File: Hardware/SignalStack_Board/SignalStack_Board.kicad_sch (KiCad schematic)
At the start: 64 parts, among them J1 Molex_uF_SV_06, J2 RJ45_LED_Shielded, J3 Molex_uF_SV_06, Q1 SI4156DY, Q2 SI4156DY, Q3 SI4156DY, Q4 SI4156DY, Q5 SI4156DY, Q6 SI4156DY, Q7 SI4156DY, Q8 SI4156DY, U1 OKI, U2 SMAJ12CA, U3 Teensy4.1_DEV-16771, U4 TSR_1-2450, U5 IRS2005S, U6 IRS2005S, U8 IRS2005S, U9 IRS2005S

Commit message: Worked on layout
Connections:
- net IMU Data is gone; now on net I2C SDA: U3.18 (A4)
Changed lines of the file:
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@@
     )
   )
-  (global_label "IMU Data" (shape input) (at 31.75 166.37 180) (fields_autoplaced)
+  (global_label "I2C SDA" (shape input) (at 31.75 166.37 180) (fields_autoplaced)
     (effects (font (size 1.27 1.27)) (justify right))
-    (property "Intersheet References" "${INTERSHEET_REFS}" (id 0) (at 20.6888 166.2906 0)
+    (property "Intersheet References" "${INTERSHEET_REFS}" (id 0) (at 21.7169 166.2906 0)
       (effects (font (size 1.27 1.27)) (justify right) hide)
     )

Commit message: Started BOM
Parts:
- Conn1, Conn2, Conn3: footprint MRDT_Connectors:Anderson_2_Horizontal_Side_by_Side -> MRDT_Connectors:Square_Anderson_2_H_Side_By_Side
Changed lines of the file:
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@@
       (effects (font (size 1.524 1.524)))
     )
-    (property "Footprint" "MRDT_Connectors:Anderson_2_Horizontal_Side_by_Side" (id 2) (at 15.24 39.37 0)
+    (property "Footprint" "MRDT_Connectors:Square_Anderson_2_H_Side_By_Side" (id 2) (at 15.24 39.37 0)
       (effects (font (size 1.524 1.524)) hide)
     )
@@
       (effects (font (size 1.524 1.524)))
     )
-    (property "Footprint" "MRDT_Connectors:Anderson_2_Horizontal_Side_by_Side" (id 2) (at 209.55 52.07 0)
+    (property "Footprint" "MRDT_Connectors:Square_Anderson_2_H_Side_By_Side" (id 2) (at 209.55 52.07 0)
       (effects (font (size 1.524 1.524)) hide)
     )
@@
       (effects (font (size 1.524 1.524)))
     )
-    (property "Footprint" "MRDT_Connectors:Anderson_2_Horizontal_Side_by_Side" (id 2) (at 209.55 102.87 0)
+    (property "Footprint" "MRDT_Connectors:Square_Anderson_2_H_Side_By_Side" (id 2) (at 209.55 102.87 0)
       (effects (font (size 1.524 1.524)) hide)
     )
@@
       (effects (font (size 1.524 1.524)))
     )
-    (property "Footprint" "MRDT_Connectors:Anderson_2_Horizontal_Side_by_Side" (id 2) (at 15.24 52.07 0)
+    (property "Footprint" "MRDT_Connectors:Square_Anderson_2_H_Side_By_Side" (id 2) (at 15.24 52.07 0)
       (effects (font (size 1.524 1.524)) hide)
     )
@@
       (effects (font (size 1.524 1.524)) (justify right))
     )
-    (property "Footprint" "MRDT_Connectors:Anderson_2_Horizontal_Side_by_Side" (id 2) (at 207.01 19.05 0)
+    (property "Footprint" "MRDT_Connectors:Square_Anderson_2_H_Side_By_Side" (id 2) (at 207.01 19.05 0)
       (effects (font (size 1.524 1.524)) hide)
     )
@@
       (effects (font (size 1.524 1.524)) (justify right))
     )
-    (property "Footprint" "MRDT_Connectors:Anderson_2_Horizontal_Side_by_Side" (id 2) (at 207.01 69.85 0)
+    (property "Footprint" "MRDT_Connectors:Square_Anderson_2_H_Side_By_Side" (id 2) (at 207.01 69.85 0)
       (effects (font (size 1.524 1.524)) hide)
     )
@@
     )
     (path "/c059550b-e967-4b7c-8d54-2cc4b7e0eff1"
-      (reference "Conn1") (unit 1) (value "AndersonPP") (footprint "MRDT_Connectors:Anderson_2_Horizontal_Side_by_Side")
+      (reference "Conn1") (unit 1) (value "AndersonPP") (footprint "MRDT_Connectors:Square_Anderson_2_H_Side_By_Side")
     )
     (path "/4470fd7a-32a9-4a7f-937a-98c8610c7077"
-      (reference "Conn1") (unit 2) (value "AndersonPP") (footprint "MRDT_Connectors:Anderson_2_Horizontal_Side_by_Side")
+      (reference "Conn1") (unit 2) (value "AndersonPP") (footprint "MRDT_Connectors:Square_Anderson_2_H_Side_By_Side")
     )
     (path "/f402e432-547b-44fa-9c6b-b785a1b7d57e"
-      (reference "Conn2") (unit 1) (value "AndersonPP") (footprint "MRDT_Connectors:Anderson_2_Horizontal_Side_by_Side")
+      (reference "Conn2") (unit 1) (value "AndersonPP") (footprint "MRDT_Connectors:Square_Anderson_2_H_Side_By_Side")
     )
     (path "/7f2e505c-6f2f-471a-8048-b70c1151c3de"
-      (reference "Conn2") (unit 2) (value "AndersonPP") (footprint "MRDT_Connectors:Anderson_2_Horizontal_Side_by_Side")
+      (reference "Conn2") (unit 2) (value "AndersonPP") (footprint "MRDT_Connectors:Square_Anderson_2_H_Side_By_Side")
     )
     (path "/f66c17f9-1ad2-418f-8418-6459a4b4a42b"
-      (reference "Conn3") (unit 1) (value "AndersonPP") (footprint "MRDT_Connectors:Anderson_2_Horizontal_Side_by_Side")
+      (reference "Conn3") (unit 1) (value "AndersonPP") (footprint "MRDT_Connectors:Square_Anderson_2_H_Side_By_Side")
     )
     (path "/b6d93951-9299-41a0-8a04-6f5e517005d6"
-      (reference "Conn3") (unit 2) (value "AndersonPP") (footprint "MRDT_Connectors:Anderson_2_Horizontal_Side_by_Side")
+      (reference "Conn3") (unit 2) (value "AndersonPP") (footprint "MRDT_Connectors:Square_Anderson_2_H_Side_By_Side")
     )
     (path "/49a02109-597c-409b-9a51-a35132935b24"

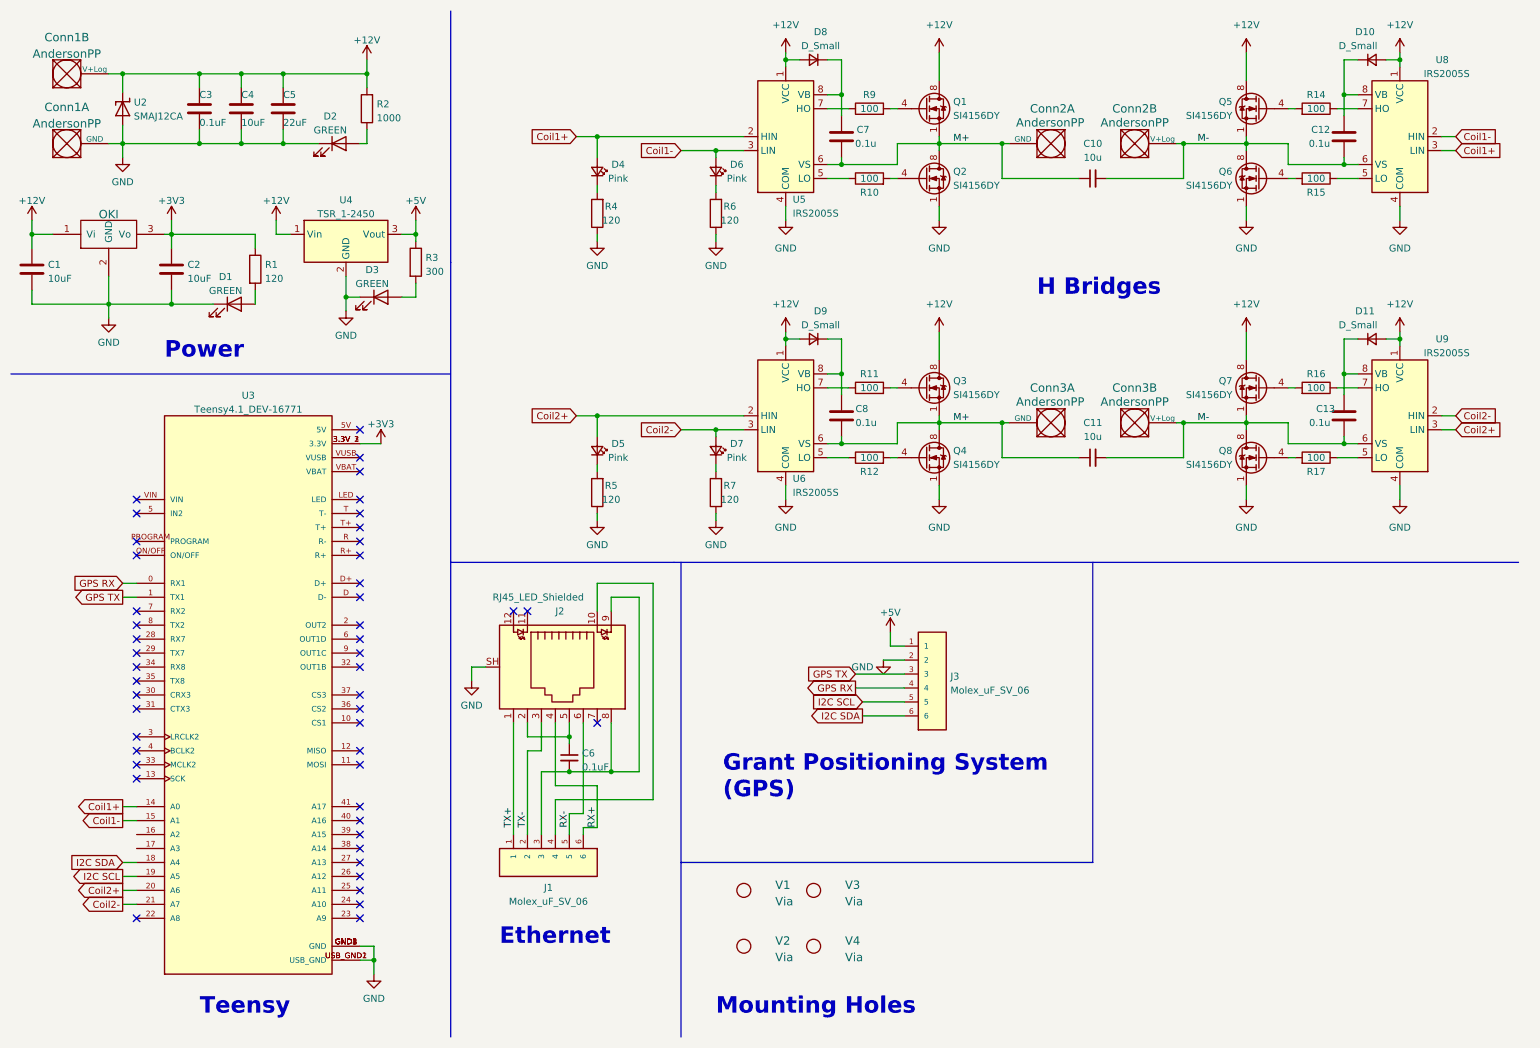
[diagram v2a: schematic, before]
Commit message: Fixed schematic H bridges
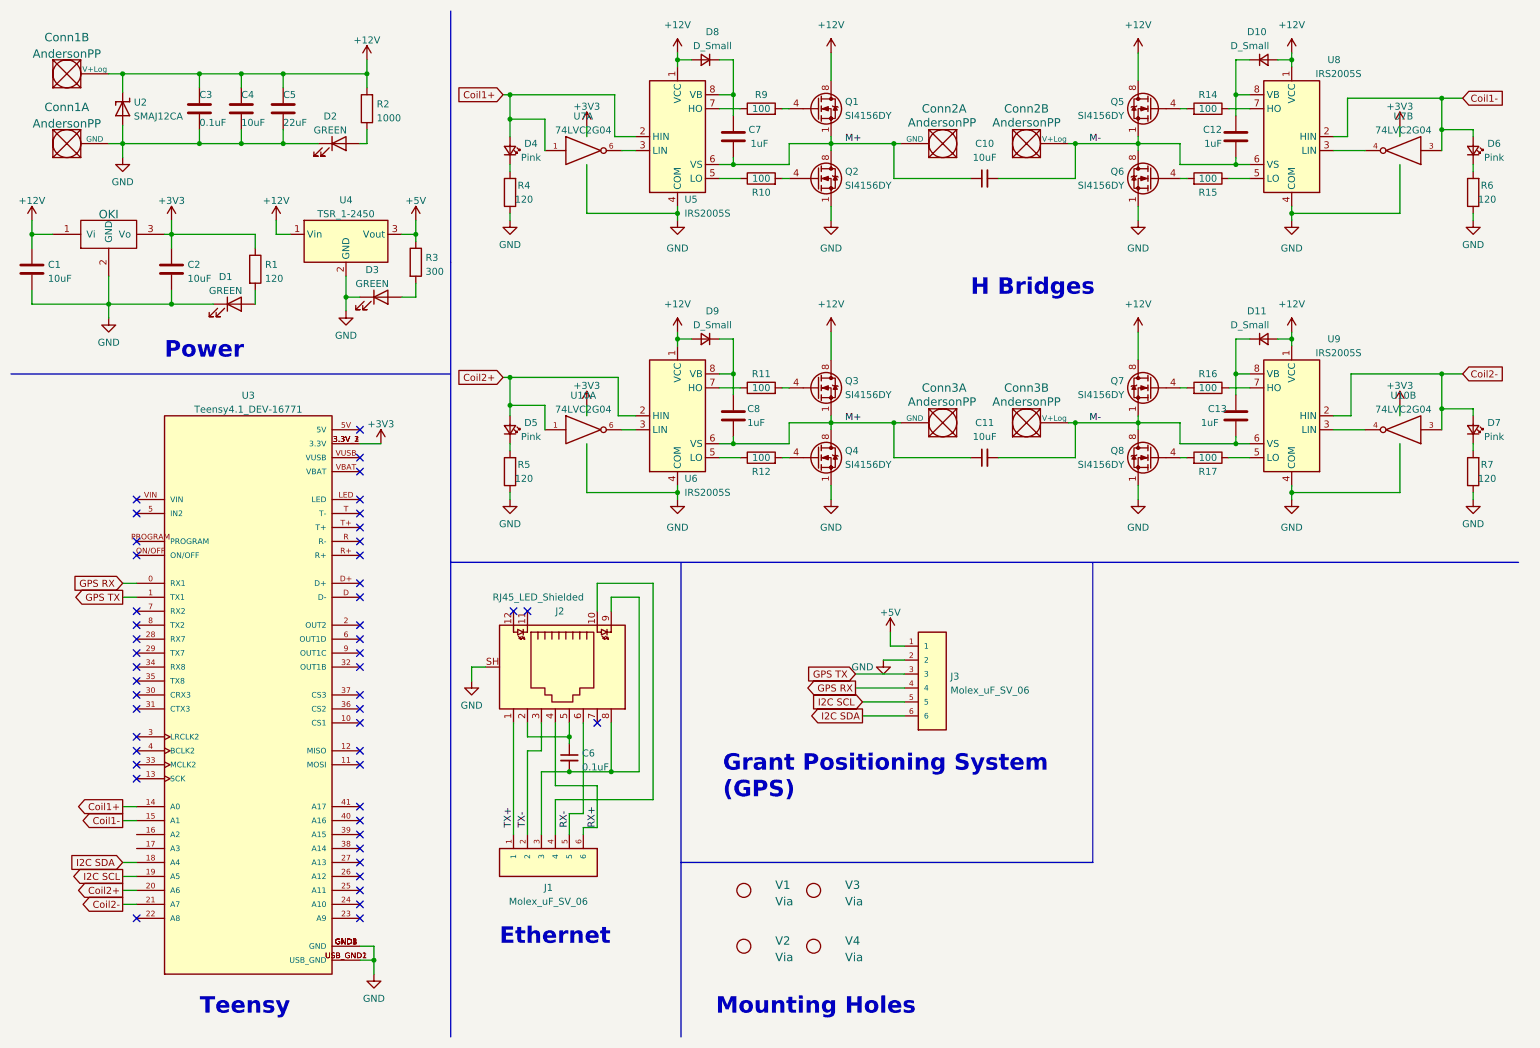
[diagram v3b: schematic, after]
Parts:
- added U10, U7: 74LVC2G04, symbol 74xGxx:74LVC2G04
- C10, C11: value 10u -> 10uF
- C12, C13, C7, C8: value 0.1u -> 1uF
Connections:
- net GND is gone; now on net +3V3: C1.2, C2.2, C3.2, C4.2, C5.2, Conn1.1 (GND), D1.1 (K), D2.1 (K), D3.1 (K), J2.SH, J3.2, Q2.1 (S), Q2.2 (S), Q2.3 (S), Q4.1 (S), Q4.2 (S), Q4.3 (S), Q6.1 (S), Q6.2 (S), Q6.3 (S), Q8.1 (S), Q8.2 (S), Q8.3 (S), R4.1, R5.1, R6.1, R7.1, U1.2 (GND), U2.A, U3.GND1 (GND), U3.GND2 (GND), U3.GND3 (GND), U3.GND4 (GND), U3.GND5 (GND), U3.USB_GND1 (USB_GND), U3.USB_GND2 (USB_GND), U4.2 (GND), U5.4 (COM), U6.4 (COM), U8.4 (COM), U9.4 (COM)
- net +3V3: now also U10.2 (GND), U10.2 (GND), U10.5 (VCC), U10.5 (VCC), U7.2 (GND), U7.2 (GND), U7.5 (VCC), U7.5 (VCC)
- net Coil1+: now also U7.1; no longer U8.3 (LIN)
- net Coil1-: now also U7.3; no longer U5.3 (LIN)
- net Coil2+: now also U10.1; no longer U9.3 (LIN)
- net Coil2-: now also U10.3; no longer U6.3 (LIN)
- new net: U10.4, U9.3 (LIN)
- new net: U10.6, U6.3 (LIN)
- new net: U5.3 (LIN), U7.6
- new net: U7.4, U8.3 (LIN)
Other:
- moved on the sheet: C10, C11, C12, C13, C7, C8, Conn2A, Conn2B, Conn3A, Conn3B, D10, D11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

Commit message: Revert "Fixed schematic H bridges"
This reverts commit 8f9c486149575b4472c9dc32ce7c4bbd756e07e9.
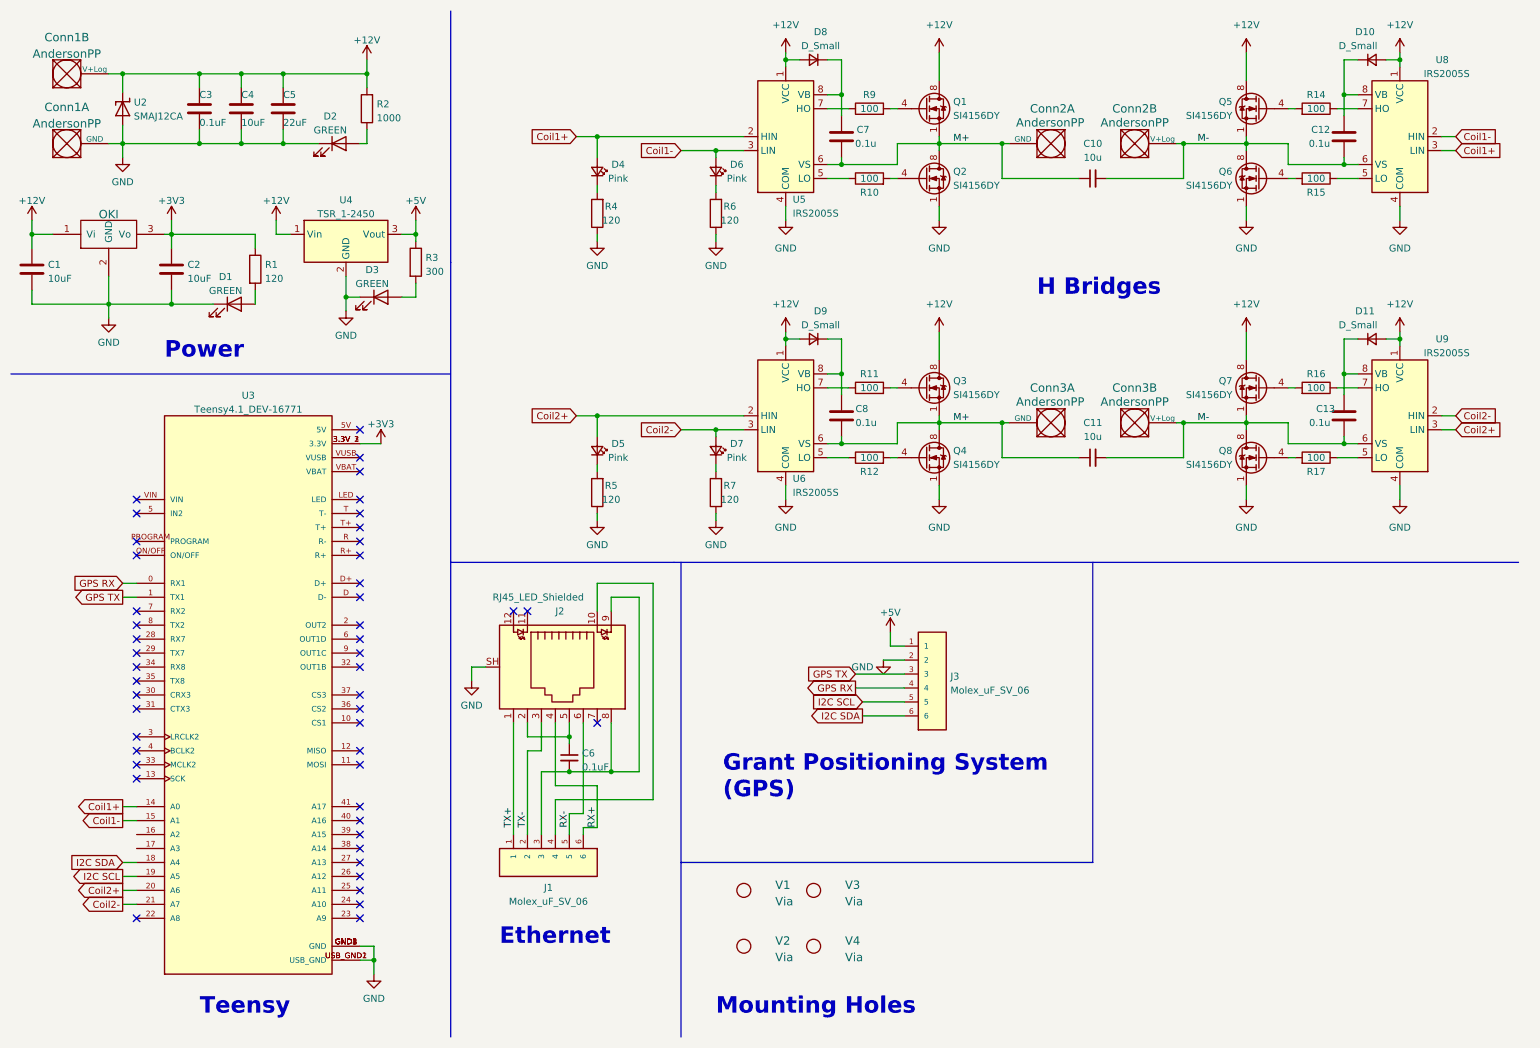
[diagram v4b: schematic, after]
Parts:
- removed U10, U7: 74LVC2G04, symbol 74xGxx:74LVC2G04
- C10, C11: value 10uF -> 10u
- C12, C13, C7, C8: value 1uF -> 0.1u
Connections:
- net +3V3: no longer C1.2, C2.2, C3.2, C4.2, C5.2, Conn1.1 (GND), D1.1 (K), D2.1 (K), D3.1 (K), J2.SH, J3.2, Q2.1 (S), Q2.2 (S), Q2.3 (S), Q4.1 (S), Q4.2 (S), Q4.3 (S), Q6.1 (S), Q6.2 (S), Q6.3 (S), Q8.1 (S), Q8.2 (S), Q8.3 (S), R4.1, R5.1, R6.1, R7.1, U1.2 (GND), U2.A, U3.GND1 (GND), U3.GND2 (GND), U3.GND3 (GND), U3.GND4 (GND), U3.GND5 (GND), U3.USB_GND1 (USB_GND), U3.USB_GND2 (USB_GND), U4.2 (GND), U5.4 (COM), U6.4 (COM), U8.4 (COM), U9.4 (COM)
- net Coil1+: now also U8.3 (LIN)
- net Coil1-: now also U5.3 (LIN)
- net Coil2+: now also U9.3 (LIN)
- net Coil2-: now also U6.3 (LIN)
- new net GND: C1.2, C2.2, C3.2, C4.2, C5.2, Conn1.1 (GND), D1.1 (K), D2.1 (K), D3.1 (K), J2.SH, J3.2, Q2.1 (S), Q2.2 (S), Q2.3 (S), Q4.1 (S), Q4.2 (S), Q4.3 (S), Q6.1 (S), Q6.2 (S), Q6.3 (S), Q8.1 (S), Q8.2 (S), Q8.3 (S), R4.1, R5.1, R6.1, R7.1, U1.2 (GND), U2.A, U3.GND1 (GND), U3.GND2 (GND), U3.GND3 (GND), U3.GND4 (GND), U3.GND5 (GND), U3.USB_GND1 (USB_GND), U3.USB_GND2 (USB_GND), U4.2 (GND), U5.4 (COM), U6.4 (COM), U8.4 (COM), U9.4 (COM)
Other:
- moved on the sheet: C10, C11, C12, C13, C7, C8, Conn2A, Conn2B, Conn3A, Conn3B, D10, D11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

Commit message: Fixed H Bridges
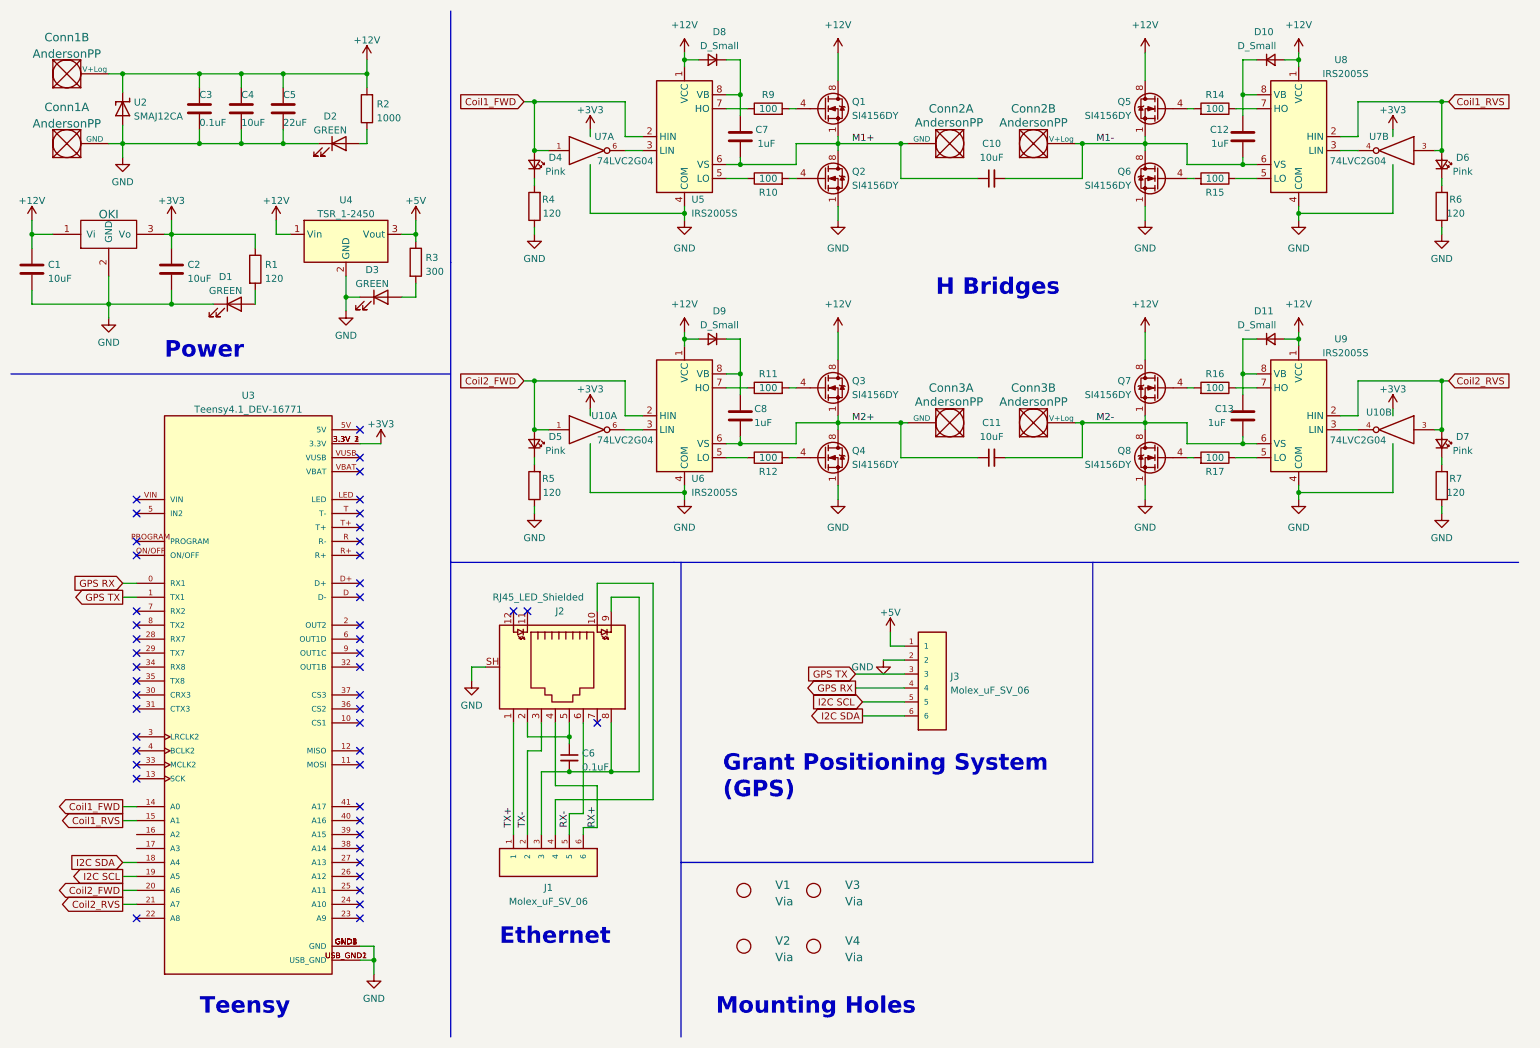
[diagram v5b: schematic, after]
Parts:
- added U10, U7: 74LVC2G04, Package_TO_SOT_SMD:SOT-23-6_Handsoldering, symbol 74xGxx:74LVC2G04
- C10, C11: value 10u -> 10uF
- C12, C13, C7, C8: value 0.1u -> 1uF
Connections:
- net +3V3: now also U10.5 (VCC), U10.5 (VCC), U7.5 (VCC), U7.5 (VCC)
- net GND: now also U10.2 (GND), U10.2 (GND), U7.2 (GND), U7.2 (GND)
- net Coil1+ renamed Coil1_FWD
- net Coil1_FWD: now also U7.1; no longer U8.3 (LIN)
- net Coil1- renamed Coil1_RVS
- net Coil1_RVS: now also U7.3; no longer U5.3 (LIN)
- net Coil2+ renamed Coil2_FWD
- net Coil2_FWD: now also U10.1; no longer U9.3 (LIN)
- net Coil2- renamed Coil2_RVS
- net Coil2_RVS: now also U10.3; no longer U6.3 (LIN)
- net M+ renamed M1+
- net M1+: no longer C11.1, C8.2, Conn3.1 (GND), Q3.1 (S), Q3.2 (S), Q3.3 (S), Q4.5 (D), Q4.6 (D), Q4.7 (D), Q4.8 (D), U6.6 (VS)
- net M- renamed M1-
- net M1-: no longer C11.2, C13.2, Conn3.2 (V+Log), Q7.1 (S), Q7.2 (S), Q7.3 (S), Q8.5 (D), Q8.6 (D), Q8.7 (D), Q8.8 (D), U9.6 (VS)
- new net: U10.6, U6.3 (LIN)
- new net: U10.4, U9.3 (LIN)
- new net: U5.3 (LIN), U7.6
- new net: U7.4, U8.3 (LIN)
- new net M2+: C11.1, C8.2, Conn3.1 (GND), Q3.1 (S), Q3.2 (S), Q3.3 (S), Q4.5 (D), Q4.6 (D), Q4.7 (D), Q4.8 (D), U6.6 (VS)
- new net M2-: C11.2, C13.2, Conn3.2 (V+Log), Q7.1 (S), Q7.2 (S), Q7.3 (S), Q8.5 (D), Q8.6 (D), Q8.7 (D), Q8.8 (D), U9.6 (VS)
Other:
- moved on the sheet: C10, C11, C12, C13, C7, C8, Conn2A, Conn2B, Conn3A, Conn3B, D10, D11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

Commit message: Fixed traces
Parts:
- U3: footprint MRDT_Shields:Teensy_4_1_Vertical -> MRDT_Shields:Teensy_4_1_Bare
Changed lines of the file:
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@@
     (property "Reference" "U3" (id 0) (at 54.61 81.3902 0))
     (property "Value" "Teensy4.1_DEV-16771" (id 1) (at 54.61 83.9271 0))
-    (property "Footprint" "MRDT_Shields:Teensy_4_1_Vertical" (id 2) (at 107.95 143.51 0)
+    (property "Footprint" "MRDT_Shields:Teensy_4_1_Bare" (id 2) (at 107.95 143.51 0)
       (effects (font (size 1.27 1.27)) (justify left bottom) hide)
     )
@@
     )
     (path "/5e3cc7ae-ad29-49d8-8135-a249683c0810"
-      (reference "U3") (unit 1) (value "Teensy4.1_DEV-16771") (footprint "MRDT_Shields:Teensy_4_1_Vertical")
+      (reference "U3") (unit 1) (value "Teensy4.1_DEV-16771") (footprint "MRDT_Shields:Teensy_4_1_Bare")
     )
     (path "/923b1e72-1c68-400a-b7fe-1ed58e70a35d"

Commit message: Began Rev2 work
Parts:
- removed J1: Molex_uF_SV_06, Connector_PinHeader_2.00mm:PinHeader_2x03_P2.00mm_Vertical, symbol MRDT_Connectors:Molex_uF_SV_06
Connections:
- net Coil2_FWD: now also U3.22 (A8); no longer U3.20 (A6)
- net Coil2_RVS: now also U3.23 (A9); no longer U3.21 (A7)
- net GND: now also C6.2, J2.8, J2.9
- net RX+: now also U3.R+
- net RX-: now also U3.R (R-)
- net TX+: now also U3.T+
- net TX-: now also U3.T (T-)
- net LED: now reaches U3.LED
- net LED: now also J2.10
- no-connect marks 48 -> 45
